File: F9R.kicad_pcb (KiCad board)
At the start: 4 copper layers, 90 x 50 mm, 73 parts, among them J1 JST_GH, J2 Molex_PicoBlade, J3 CONN_06NO_SILK_FEMALE_PTH, J4 Conn_01x06, P1 USB_C_Plug_USB2.0, U1 ZED-F9R, U2 DUAL-OPTO_HCPL-073L, U3 LD1117S33TR, U4 UHS_INVERTER_SCHMITT_TRIGGERS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, U5 UHS_INVERTER_SCHMITT_TRIGGERS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

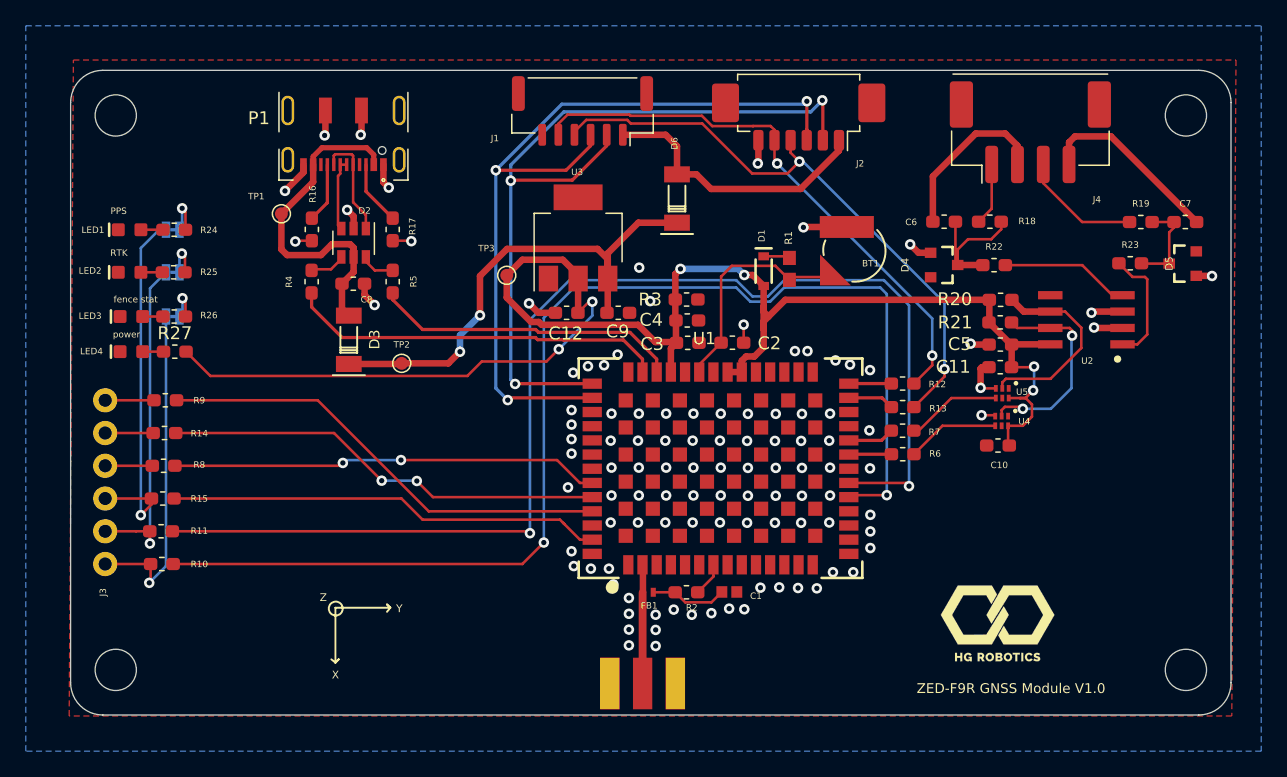
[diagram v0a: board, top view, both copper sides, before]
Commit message: edited silk screen to 0.5, 0.5, 0.1 size
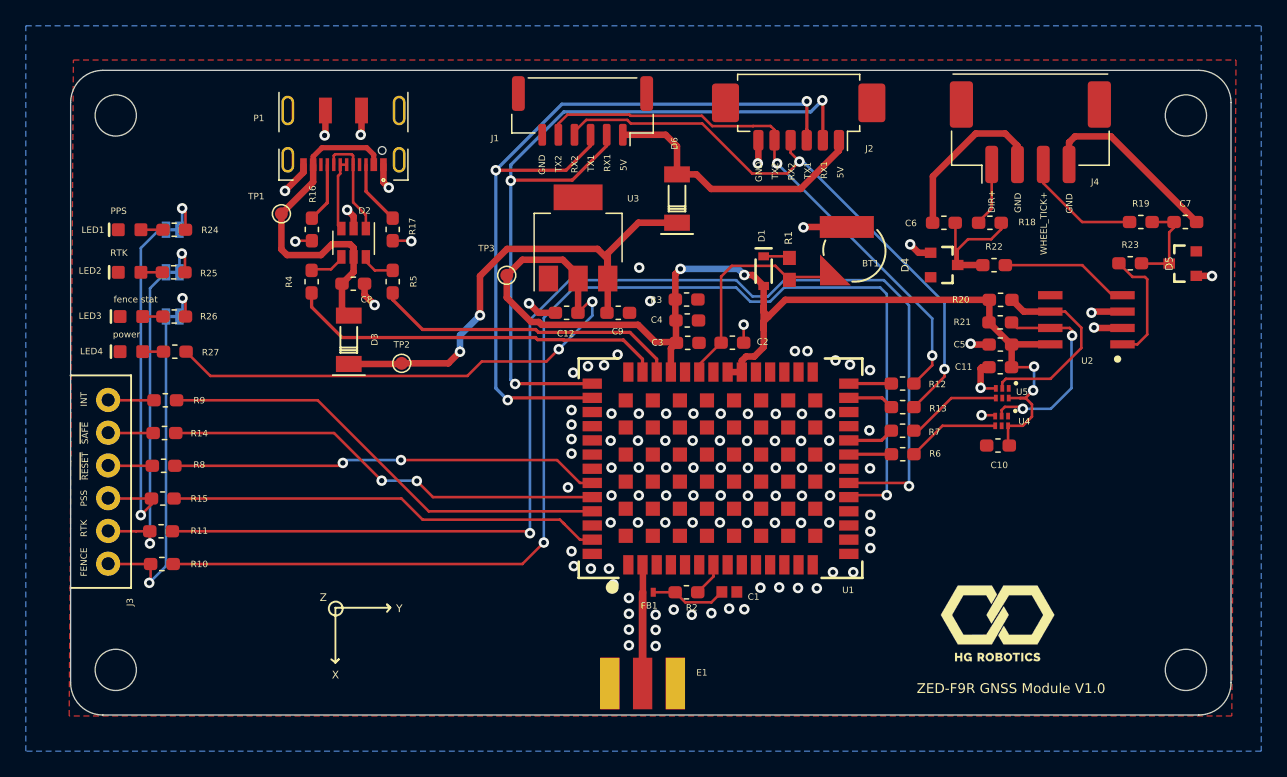
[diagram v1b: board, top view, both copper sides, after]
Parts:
- moved J3 0.23 mm to (122.9, 88.3)
- moved C6 0.09 mm to (187.7, 61.8)
- moved R18 0.08 mm to (191.3, 61.8)
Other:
- board text added: "5V"
- board text added: "DIR+"
- board text added: "FENCE"
- board text added: "GND"
- board text added: "INT"
- board text added: "PSS"
- board text added: "RX1"
- board text added: "RX2"
- board text added: "TX1"
- board text added: "TX2"
- board text added: "WHEEL_TICK+"
- board text added: "~RESET"
- board text added: "~SAFE"
